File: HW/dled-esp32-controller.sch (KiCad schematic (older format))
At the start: 35 parts, among them J1 PinsI2C, J2 PinsDbg, J3 DLED, J4 swRes, J5 PinsExp, J9 Power5V, Q1 STD46P4LLF6, Q2 IRLML2502, SW1 BootBtn, U1 ESP-WROOM-32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

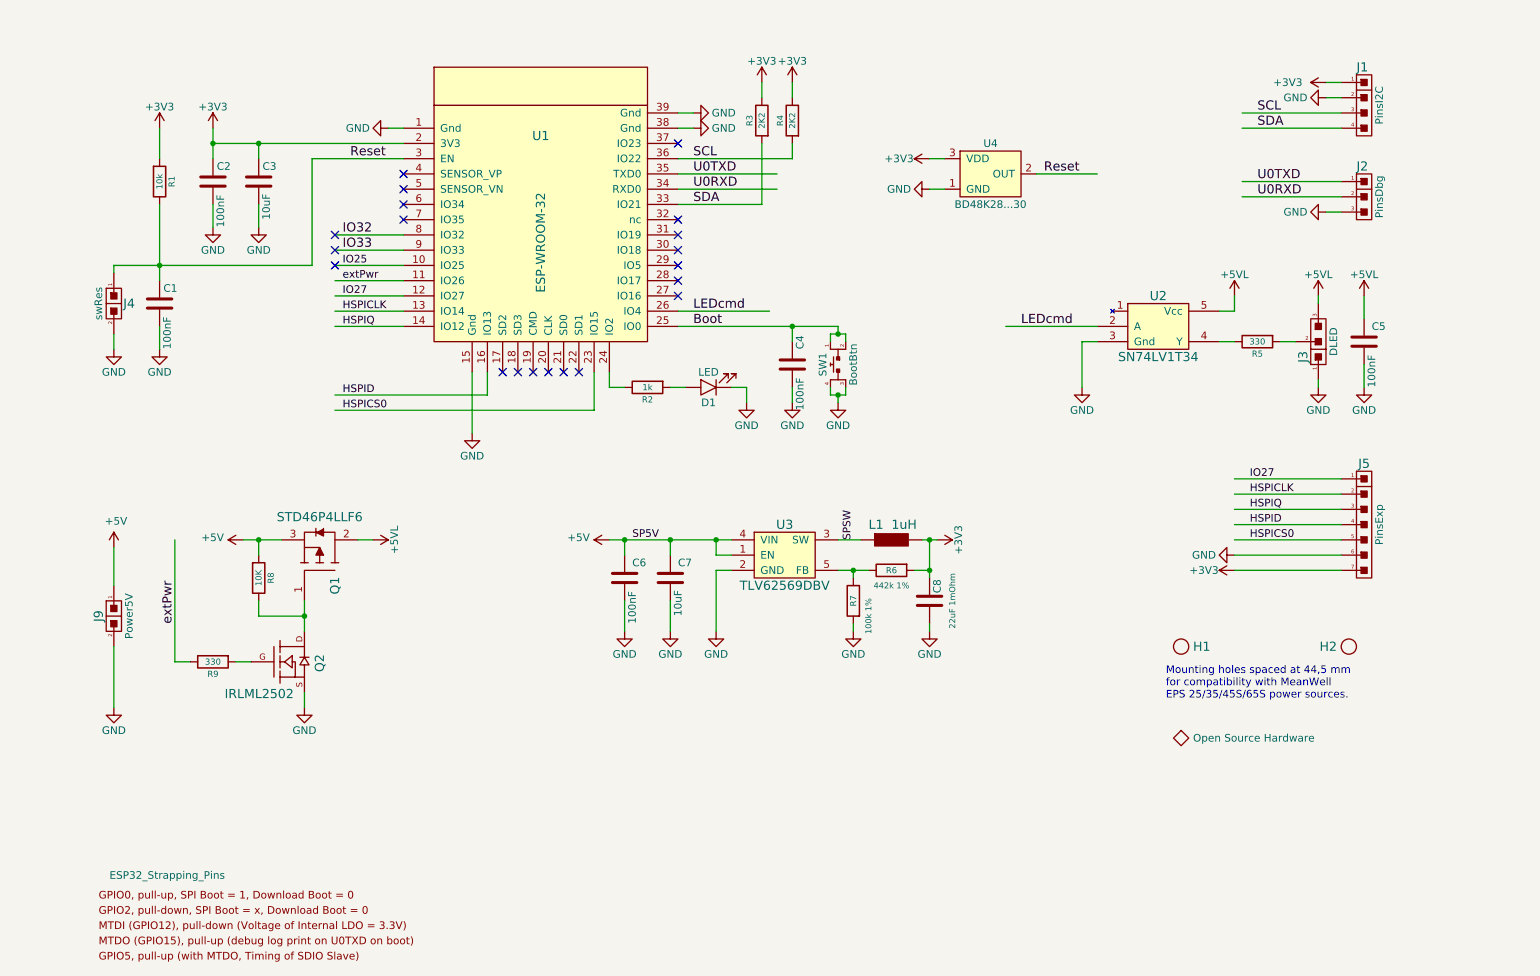
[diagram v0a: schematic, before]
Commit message: Modifies the design for two outputs
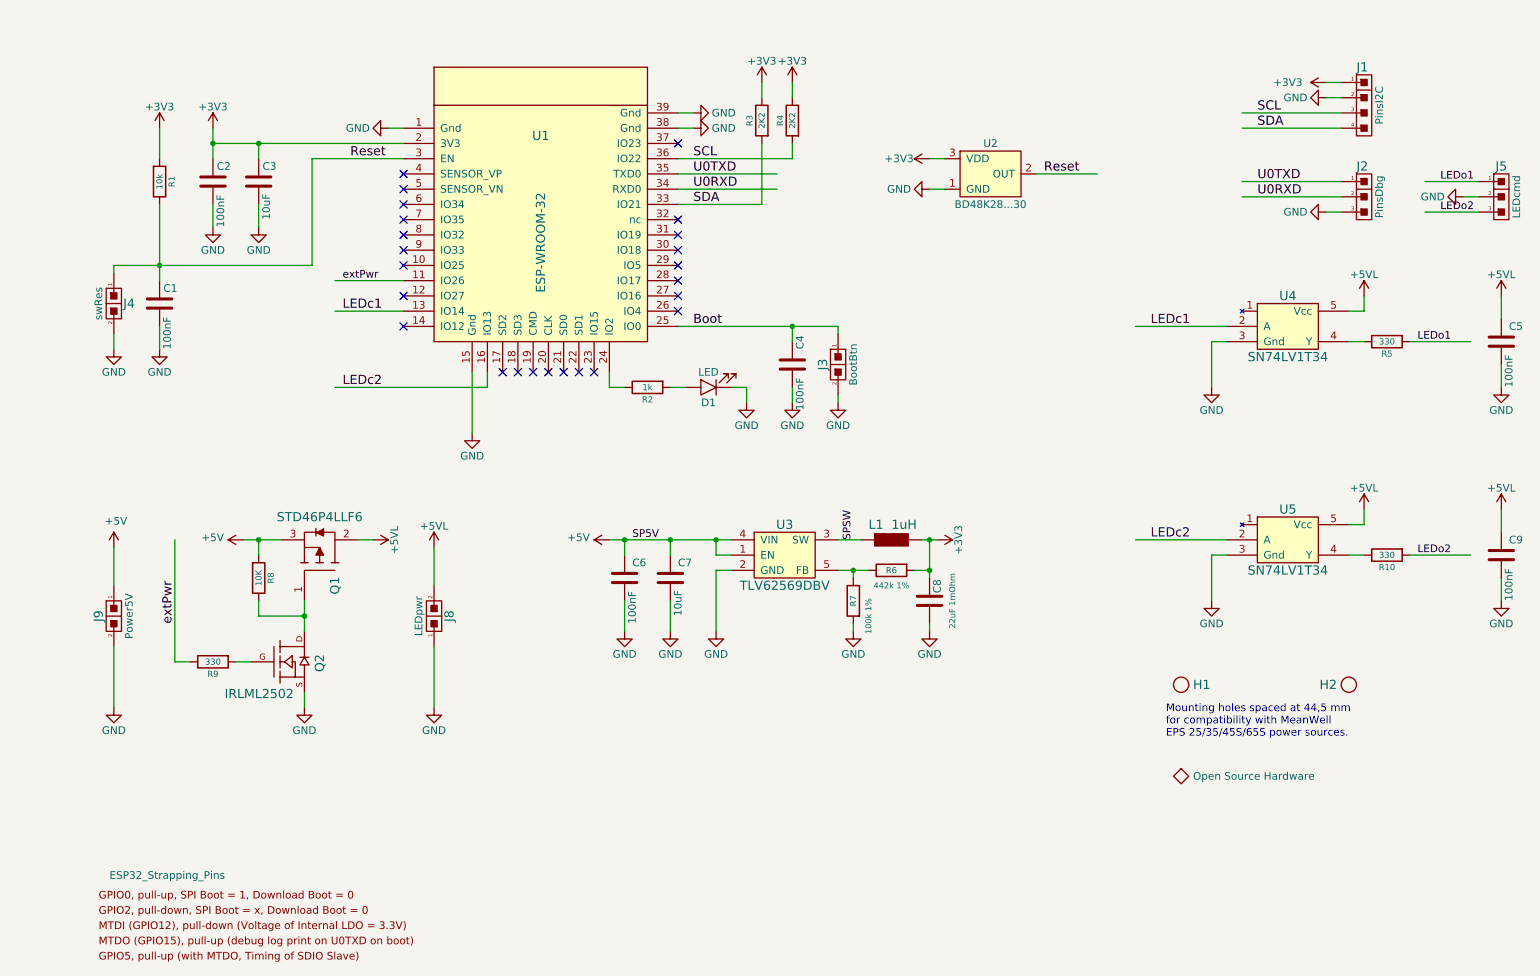
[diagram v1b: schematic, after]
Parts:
- removed J3: DLED, CalinConnectors:DG301-5-3, symbol calin:CS_3n
- removed J5: PinsExp, CalinConnectors:Pin_Header_Straight_1x07, symbol calin:CS_7
- removed SW1: BootBtn, CalinGeneric:SW-Push-4, symbol calin:SW-Push4
- added C9: 100nF, CalinGeneric:C0805HS, symbol Device:C
- added J3: BootBtn, CalinConnectors:Pin_Header_Straight_1x02, symbol calin:CS_2
- added J5: LEDcmd, CalinConnectors:Pin_Header_Straight_1x03, symbol calin:CS_3
- added J8: LEDpwr, CalinConnectors:DG301-5-2, symbol calin:CS_2
- added R10: 330, CalinGeneric:R0805HS, symbol calin:R
- added U5: SN74LV1T34, CalinGeneric:SOT-23-5-HS, symbol calin:SN74LV1T34
- renumbered U4 to U2, U2 to U4
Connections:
- net labels added: LEDc1, LEDc2, LEDo1, LEDo2
- net labels removed: HSPICLK, HSPICS0, HSPID, HSPIQ, IO25, IO27, IO32, IO33, LEDcmd
- wire segments 125 -> 114
- no-connect marks 20 -> 24
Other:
- moved on the sheet: C5, H1, H2, R5, U4

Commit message: Adds an extension header and improves many PCB traces.
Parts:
- added J6: PinsExt, CalinConnectors:Pin_Header_Straight_1x05, symbol calin:CS_5
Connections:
- net labels added: 25, 32, 33
- wire segments 114 -> 122
- no-connect marks 24 -> 21
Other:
- moved on the sheet: J1, J2, J5
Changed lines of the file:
@@
 Sheet 1 1
 Title "dled-esp32-controller"
-Date "2019-03-11"
-Rev "7"
+Date "2019-03-25"
+Rev "8"
 Comp "Calin Radoni"
 Comment1 "https://github.com/CalinRadoni/dled-esp32-controller"
@@
 L power:GND #PWR0106
 U 1 1 5C31FA5D
-P 9150 1400
-F 0 "#PWR0106" H 9150 1150 50  0001 C CNN
-F 1 "GND" V 9150 1200 50  0000 C CNN
-F 2 "" H 9150 1400 50  0000 C CNN
-F 3 "" H 9150 1400 50  0000 C CNN
-	1    9150 1400
+P 9150 1100
+F 0 "#PWR0106" H 9150 850 50  0001 C CNN
+F 1 "GND" V 9150 900 50  0000 C CNN
+F 2 "" H 9150 1100 50  0000 C CNN
+F 3 "" H 9150 1100 50  0000 C CNN
+	1    9150 1100
 	0    1    1    0
 $EndComp
@@
 L power:+3V3 #PWR0107
 U 1 1 5C31FAA4
-P 9150 1300
-F 0 "#PWR0107" H 9150 1150 50  0001 C CNN
-F 1 "+3V3" V 9150 1550 50  0000 C CNN
-F 2 "" H 9150 1300 50  0000 C CNN
-F 3 "" H 9150 1300 50  0000 C CNN
-	1    9150 1300
+P 9150 1000
+F 0 "#PWR0107" H 9150 850 50  0001 C CNN
+F 1 "+3V3" V 9150 1250 50  0000 C CNN
+F 2 "" H 9150 1000 50  0000 C CNN
+F 3 "" H 9150 1000 50  0000 C CNN
+	1    9150 1000
 	0    -1   -1   0
 $EndComp
@@
 L calin:CS_4 J1
 U 1 1 5C8662A2
-P 9400 1450
-F 0 "J1" H 9350 1700 60  0000 L CNN
-F 1 "PinsI2C" V 9500 1450 50  0000 C CNN
-F 2 "CalinConnectors:Pin_Header_Straight_1x04" H 9400 1600 60  0001 C CNN
-F 3 "" H 9400 1600 60  0000 C CNN
-	1    9400 1450
+P 9400 1150
+F 0 "J1" H 9350 1400 60  0000 L CNN
+F 1 "PinsI2C" V 9500 1150 50  0000 C CNN
+F 2 "CalinConnectors:Pin_Header_Straight_1x04" H 9400 1300 60  0001 C CNN
+F 3 "" H 9400 1300 60  0000 C CNN
+	1    9400 1150
 	1    0    0    -1
 $EndComp
@@
 L calin:CS_3 J2
 U 1 1 5C86638B
-P 9400 2050
-F 0 "J2" H 9350 2250 60  0000 L CNN
-F 1 "PinsDbg" V 9500 2050 50  0000 C CNN
-F 2 "CalinConnectors:Pin_Header_Straight_1x03" H 9400 2150 60  0001 C CNN
-F 3 "" H 9400 2150 60  0000 C CNN
-	1    9400 2050
-	1    0    0    -1
-$EndComp
-Wire Wire Line
-	9250 1500 8600 1500
+P 9400 1700
+F 0 "J2" H 9350 1900 60  0000 L CNN
+F 1 "PinsDbg" V 9500 1700 50  0000 C CNN
+F 2 "CalinConnectors:Pin_Header_Straight_1x03" H 9400 1800 60  0001 C CNN
+F 3 "" H 9400 1800 60  0000 C CNN
+	1    9400 1700
+	1    0    0    -1
+$EndComp
+Wire Wire Line
+	9250 1200 8600 1200
+Wire Wire Line
+	9250 1300 8600 1300
 Wire Wire Line
 	9250 1600 8600 1600
 Wire Wire Line
-	9250 1950 8600 1950
-Wire Wire Line
-	9250 2050 8600 2050
-Wire Wire Line
-	9150 1300 9250 1300
-Wire Wire Line
-	9150 1400 9250 1400
+	9250 1700 8600 1700
+Wire Wire Line
+	9150 1000 9250 1000
+Wire Wire Line
+	9150 1100 9250 1100
 $Comp
 L power:GND #PWR0110
 U 1 1 5C8871CD
-P 9150 2150
-F 0 "#PWR0110" H 9150 1900 50  0001 C CNN
-F 1 "GND" V 9150 1950 50  0000 C CNN
-F 2 "" H 9150 2150 50  0000 C CNN
-F 3 "" H 9150 2150 50  0000 C CNN
-	1    9150 2150
+P 9150 1800
+F 0 "#PWR0110" H 9150 1550 50  0001 C CNN
+F 1 "GND" V 9150 1600 50  0000 C CNN
+F 2 "" H 9150 1800 50  0000 C CNN
+F 3 "" H 9150 1800 50  0000 C CNN
+	1    9150 1800
 	0    1    1    0
 $EndComp
 Wire Wire Line
-	9250 2150 9150 2150
-Text Label 8700 1500 0    60   ~ 0
+	9250 1800 9150 1800
+Text Label 8700 1200 0    60   ~ 0
 SCL
+Text Label 8700 1300 0    60   ~ 0
+SDA
 Text Label 8700 1600 0    60   ~ 0
-SDA
-Text Label 8700 1950 0    60   ~ 0
 U0TXD
-Text Label 8700 2050 0    60   ~ 0
+Text Label 8700 1700 0    60   ~ 0
 U0RXD
 $Comp
@@
 	3300 5000 3300 5400
 Wire Wire Line
-	10150 1950 9800 1950
-Text Label 9900 1950 0    50   ~ 0
+	9250 2100 8600 2100
+Text Label 8700 2100 0    50   ~ 0
 LEDo1
-Text Label 9900 2150 0    50   ~ 0
+Text Label 8700 2300 0    50   ~ 0
 LEDo2
 Wire Wire Line
@@
 NoConn ~ 3100 2700
 NoConn ~ 3100 2900
-NoConn ~ 3100 2300
-NoConn ~ 3100 2400
-NoConn ~ 3100 2500
 Wire Wire Line
 	3100 2800 2650 2800
@@
 L calin:CS_3 J5
 U 1 1 5C901D00
-P 10300 2050
-F 0 "J5" H 10300 2250 60  0000 C CNN
-F 1 "LEDcmd" V 10400 2050 50  0000 C CNN
-F 2 "CalinConnectors:Pin_Header_Straight_1x03" H 10300 2150 60  0001 C CNN
-F 3 "" H 10300 2150 60  0000 C CNN
-	1    10300 2050
-	1    0    0    -1
-$EndComp
-Wire Wire Line
-	10150 2150 9800 2150
+P 9400 2200
+F 0 "J5" H 9400 2400 60  0000 C CNN
+F 1 "LEDcmd" V 9500 2200 50  0000 C CNN
+F 2 "CalinConnectors:Pin_Header_Straight_1x03" H 9400 2300 60  0001 C CNN
+F 3 "" H 9400 2300 60  0000 C CNN
+	1    9400 2200
+	1    0    0    -1
+$EndComp
+Wire Wire Line
+	9250 2300 8600 2300
 $Comp
 L power:GND #PWR0119
 U 1 1 5C9054A7
-P 10050 2050
-F 0 "#PWR0119" H 10050 1800 50  0001 C CNN
-F 1 "GND" V 10050 1850 50  0000 C CNN
-F 2 "" H 10050 2050 50  0000 C CNN
-F 3 "" H 10050 2050 50  0000 C CNN
-	1    10050 2050
+P 9150 2200
+F 0 "#PWR0119" H 9150 1950 50  0001 C CNN
+F 1 "GND" V 9150 2000 50  0000 C CNN
+F 2 "" H 9150 2200 50  0000 C CNN
+F 3 "" H 9150 2200 50  0000 C CNN
+	1    9150 2200
 	0    1    1    0
 $EndComp
 Wire Wire Line
-	10150 2050 10050 2050
+	9250 2200 9150 2200
+$Comp
+L calin:CS_5 J6
+U 1 1 5C9AC777
+P 10300 1700
+F 0 "J6" H 10300 2000 60  0000 C CNN
+F 1 "PinsExt" V 10400 1700 50  0000 C CNN
+F 2 "CalinConnectors:Pin_Header_Straight_1x05" H 10300 1900 60  0001 C CNN
+F 3 "" H 10300 1900 60  0000 C CNN
+	1    10300 1700
+	1    0    0    -1
+$EndComp
+$Comp
+L power:+3V3 #PWR0120
+U 1 1 5C9AC805
+P 10050 1900
+F 0 "#PWR0120" H 10050 1750 50  0001 C CNN
+F 1 "+3V3" V 10050 2150 50  0000 C CNN
+F 2 "" H 10050 1900 50  0000 C CNN
+F 3 "" H 10050 1900 50  0000 C CNN
+	1    10050 1900
+	0    -1   -1   0
+$EndComp
+$Comp
+L power:GND #PWR0121
+U 1 1 5C9AC85C
+P 10050 1500
+F 0 "#PWR0121" H 10050 1250 50  0001 C CNN
+F 1 "GND" V 10050 1300 50  0000 C CNN
+F 2 "" H 10050 1500 50  0000 C CNN
+F 3 "" H 10050 1500 50  0000 C CNN
+	1    10050 1500
+	0    1    1    0
+$EndComp
+Wire Wire Line
+	10150 1500 10050 1500
+Wire Wire Line
+	10150 1900 10050 1900
+Wire Wire Line
+	10150 1800 9650 1800
+Wire Wire Line
+	10150 1700 9650 1700
+Wire Wire Line
+	10150 1600 9650 1600
+Text Label 9700 1600 0    50   ~ 0
+32
+Text Label 9700 1700 0    50   ~ 0
+33
+Text Label 9700 1800 0    50   ~ 0
+25
+Wire Wire Line
+	3100 2300 2650 2300
+Wire Wire Line
+	3100 2400 2650 2400
+Wire Wire Line
+	3100 2500 2650 2500
+Text Label 2700 2300 0    50   ~ 0
+32
+Text Label 2700 2400 0    50   ~ 0
+33
+Text Label 2700 2500 0    50   ~ 0
+25
 $EndSCHEMATC

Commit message: Modifies the schematic to add a second extension connector
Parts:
- added J7: PinsExt2, CalinConnectors:Pin_Header_Straight_1x03, symbol calin:CS_3
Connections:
- net labels added: RTC10
- wire segments 122 -> 126
- no-connect marks 21 -> 20
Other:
- moved on the sheet: J6
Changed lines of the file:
@@
 Sheet 1 1
 Title "dled-esp32-controller"
-Date "2019-03-25"
-Rev "8"
+Date "2019-03-27"
+Rev "9"
 Comp "Calin Radoni"
 Comment1 "https://github.com/CalinRadoni/dled-esp32-controller"
@@
 Text Label 2700 3300 0    60   ~ 0
 LEDc2
-NoConn ~ 4900 2800
 NoConn ~ 4350 3200
 NoConn ~ 3100 2700
@@
 L calin:CS_5 J6
 U 1 1 5C9AC777
-P 10300 1700
-F 0 "J6" H 10300 2000 60  0000 C CNN
-F 1 "PinsExt" V 10400 1700 50  0000 C CNN
-F 2 "CalinConnectors:Pin_Header_Straight_1x05" H 10300 1900 60  0001 C CNN
-F 3 "" H 10300 1900 60  0000 C CNN
-	1    10300 1700
+P 10300 1450
+F 0 "J6" H 10300 1750 60  0000 C CNN
+F 1 "PinsExt" V 10400 1450 50  0000 C CNN
+F 2 "CalinConnectors:Pin_Header_Straight_1x05" H 10300 1650 60  0001 C CNN
+F 3 "" H 10300 1650 60  0000 C CNN
+	1    10300 1450
 	1    0    0    -1
 $EndComp
@@
 L power:+3V3 #PWR0120
 U 1 1 5C9AC805
-P 10050 1900
-F 0 "#PWR0120" H 10050 1750 50  0001 C CNN
-F 1 "+3V3" V 10050 2150 50  0000 C CNN
-F 2 "" H 10050 1900 50  0000 C CNN
-F 3 "" H 10050 1900 50  0000 C CNN
-	1    10050 1900
+P 10050 1650
+F 0 "#PWR0120" H 10050 1500 50  0001 C CNN
+F 1 "+3V3" V 10050 1900 50  0000 C CNN
+F 2 "" H 10050 1650 50  0000 C CNN
+F 3 "" H 10050 1650 50  0000 C CNN
+	1    10050 1650
 	0    -1   -1   0
 $EndComp
@@
 L power:GND #PWR0121
 U 1 1 5C9AC85C
-P 10050 1500
-F 0 "#PWR0121" H 10050 1250 50  0001 C CNN
-F 1 "GND" V 10050 1300 50  0000 C CNN
-F 2 "" H 10050 1500 50  0000 C CNN
-F 3 "" H 10050 1500 50  0000 C CNN
-	1    10050 1500
+P 10050 1250
+F 0 "#PWR0121" H 10050 1000 50  0001 C CNN
+F 1 "GND" V 10050 1050 50  0000 C CNN
+F 2 "" H 10050 1250 50  0000 C CNN
+F 3 "" H 10050 1250 50  0000 C CNN
+	1    10050 1250
 	0    1    1    0
 $EndComp
 Wire Wire Line
-	10150 1500 10050 1500
-Wire Wire Line
-	10150 1900 10050 1900
-Wire Wire Line
-	10150 1800 9650 1800
-Wire Wire Line
-	10150 1700 9650 1700
-Wire Wire Line
-	10150 1600 9650 1600
-Text Label 9700 1600 0    50   ~ 0
+	10150 1250 10050 1250
+Wire Wire Line
+	10150 1650 10050 1650
+Wire Wire Line
+	10150 1550 9650 1550
+Wire Wire Line
+	10150 1450 9650 1450
+Wire Wire Line
+	10150 1350 9650 1350
+Text Label 9700 1350 0    50   ~ 0
 32
-Text Label 9700 1700 0    50   ~ 0
+Text Label 9700 1450 0    50   ~ 0
 33
-Text Label 9700 1800 0    50   ~ 0
+Text Label 9700 1550 0    50   ~ 0
 25
 Wire Wire Line
@@
 Text Label 2700 2500 0    50   ~ 0
 25
+$Comp
+L calin:CS_3 J7
+U 1 1 5C9C1F19
+P 10300 2200
+F 0 "J7" H 10300 2400 60  0000 C CNN
+F 1 "PinsExt2" V 10400 2200 50  0000 C CNN
+F 2 "CalinConnectors:Pin_Header_Straight_1x03" H 10300 2300 60  0001 C CNN
+F 3 "" H 10300 2300 60  0000 C CNN
+	1    10300 2200
+	1    0    0    -1
+$EndComp
+$Comp
+L power:+3V3 #PWR0122
+U 1 1 5C9C99F2
+P 10050 2100
+F 0 "#PWR0122" H 10050 1950 50  0001 C CNN
+F 1 "+3V3" V 10050 2350 50  0000 C CNN
+F 2 "" H 10050 2100 50  0000 C CNN
+F 3 "" H 10050 2100 50  0000 C CNN
+	1    10050 2100
+	0    -1   -1   0
+$EndComp
+$Comp
+L power:GND #PWR0123
+U 1 1 5C9C9A4B
+P 10050 2300
+F 0 "#PWR0123" H 10050 2050 50  0001 C CNN
+F 1 "GND" V 10050 2100 50  0000 C CNN
+F 2 "" H 10050 2300 50  0000 C CNN
+F 3 "" H 10050 2300 50  0000 C CNN
+	1    10050 2300
+	0    1    1    0
+$EndComp
+Wire Wire Line
+	10150 2100 10050 2100
+Wire Wire Line
+	10150 2300 10050 2300
+Wire Wire Line
+	10150 2200 9650 2200
+Text Label 9700 2200 0    50   ~ 0
+RTC10
+Text Label 5000 2800 0    50   ~ 0
+RTC10
+Wire Wire Line
+	4900 2800 5550 2800
 $EndSCHEMATC

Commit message: Rebuilds the PCB for the second extension connector
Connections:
- net labels added: IO4
- net labels removed: RTC10
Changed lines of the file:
@@
 	10150 2200 9650 2200
 Text Label 9700 2200 0    50   ~ 0
-RTC10
+IO4
 Text Label 5000 2800 0    50   ~ 0
-RTC10
+IO4
 Wire Wire Line
 	4900 2800 5550 2800

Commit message: Changes the 3D representation of some connectors
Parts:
- J2: footprint CalinConnectors:Pin_Header_Straight_1x03 -> CalinConnectors:Pin_Header_Straight_1x03_Cyan
- J5: footprint CalinConnectors:Pin_Header_Straight_1x03 -> CalinConnectors:Pin_Header_Straight_1x03_Yellow
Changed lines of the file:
@@
 Sheet 1 1
 Title "dled-esp32-controller"
-Date "2019-03-27"
-Rev "9"
+Date "2019-04-02"
+Rev "10"
 Comp "Calin Radoni"
 Comment1 "https://github.com/CalinRadoni/dled-esp32-controller"
@@
 F 0 "J2" H 9350 1900 60  0000 L CNN
 F 1 "PinsDbg" V 9500 1700 50  0000 C CNN
-F 2 "CalinConnectors:Pin_Header_Straight_1x03" H 9400 1800 60  0001 C CNN
+F 2 "CalinConnectors:Pin_Header_Straight_1x03_Cyan" H 9400 1800 60  0001 C CNN
 F 3 "" H 9400 1800 60  0000 C CNN
 	1    9400 1700
@@
 F 0 "J5" H 9400 2400 60  0000 C CNN
 F 1 "LEDcmd" V 9500 2200 50  0000 C CNN
-F 2 "CalinConnectors:Pin_Header_Straight_1x03" H 9400 2300 60  0001 C CNN
+F 2 "CalinConnectors:Pin_Header_Straight_1x03_Yellow" H 9400 2300 60  0001 C CNN
 F 3 "" H 9400 2300 60  0000 C CNN
 	1    9400 2200

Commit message: Changes the inductor to a more correct value and the LED's resistor to a sane value
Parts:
- L1: value 1uH -> 2.2uH
- R2: value 1k -> 330
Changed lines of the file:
@@
 Title "dled-esp32-controller"
 Date "2019-04-02"
-Rev "10"
+Rev "11"
 Comp "Calin Radoni"
 Comment1 "https://github.com/CalinRadoni/dled-esp32-controller"
@@
 U 1 1 5C1BC1CD
 P 6300 4300
-F 0 "L1" H 6150 4400 60  0000 L CNN
-F 1 "1uH" H 6300 4400 60  0000 L CNN
+F 0 "L1" H 6200 4400 39  0000 C CNN
+F 1 "2.2uH" H 6400 4400 39  0000 C CNN
 F 2 "CalinGeneric:ASPI-0530HI" H 6300 4300 60  0001 C CNN
 F 3 "" H 6300 4300 60  0001 C CNN
@@
 P 4700 3300
 F 0 "R2" V 4780 3300 40  0000 C CNN
-F 1 "1k" V 4700 3300 40  0000 C CNN
+F 1 "330" V 4700 3300 40  0000 C CNN
 F 2 "CalinGeneric:R0805HS" V 4630 3300 30  0001 C CNN
 F 3 "" H 4700 3300 30  0000 C CNN
